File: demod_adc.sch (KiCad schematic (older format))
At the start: 0 parts

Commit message: Finished filters page, started demod
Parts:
- added C?: 0.1uF, ~, symbol C
- added R? (x2): 2.2k, ~, symbol R
- added T?: TRANSFO2, ~, symbol TRANSFO2
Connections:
- new net: C?.2, R?.1, R?.2, T?.2 (AB)
- new net: T?.4 (SB), T?.5 (SC)
- new net +5V: R?.1
- new net AGND: C?.1, R?.2
- new net ft_ana: T?.1 (AA)
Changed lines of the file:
@@
 LIBS:cmos4000
 LIBS:adc-dac
-LIBS:memory
 LIBS:special
 LIBS:analog_switches
@@
 LIBS:tsop
 LIBS:varistor
-LIBS:vishay
-LIBS:vishay_tsal4400_bpw85c
-LIBS:vishay-1
 LIBS:v-reg
-LIBS:v-reg-2
-LIBS:v-reg-fairchild
-LIBS:v-reg-lowdrop
 LIBS:si570
 LIBS:blackrock_components
@@
 $Descr A4 11693 8268
 encoding utf-8
-Sheet 1 5
+Sheet 5 5
 Title ""
-Date "16 oct 2014"
+Date "19 oct 2014"
 Rev ""
 Comp ""
@@
 Comment4 ""
 $EndDescr
+$Comp
+L +5V #PWR?
+U 1 1 54442E3F
+P 1700 1500
+F 0 "#PWR?" H 1700 1590 20  0001 C CNN
+F 1 "+5V" H 1700 1590 30  0000 C CNN
+F 2 "" H 1700 1500 60  0000 C CNN
+F 3 "" H 1700 1500 60  0000 C CNN
+	1    1700 1500
+	1    0    0    -1
+$EndComp
+$Comp
+L AGND #PWR?
+U 1 1 54442E45
+P 1050 2350
+F 0 "#PWR?" H 1050 2350 40  0001 C CNN
+F 1 "AGND" H 1050 2250 50  0000 C CNN
+F 2 "" H 1050 2350 60  0000 C CNN
+F 3 "" H 1050 2350 60  0000 C CNN
+	1    1050 2350
+	1    0    0    -1
+$EndComp
+$Comp
+L C C?
+U 1 1 54442E4B
+P 1350 2150
+F 0 "C?" V 1400 2250 40  0000 L CNN
+F 1 "0.1uF" V 1400 1900 40  0000 L CNN
+F 2 "~" H 1388 2000 30  0000 C CNN
+F 3 "~" H 1350 2150 60  0000 C CNN
+	1    1350 2150
+	0    -1   -1   0
+$EndComp
+Connection ~ 1650 2150
+Wire Wire Line
+	1550 2150 2550 2150
+Wire Wire Line
+	1050 2150 1050 2350
+Wire Wire Line
+	1150 2150 1050 2150
+$Comp
+L R R?
+U 1 1 54442E55
+P 1700 1850
+F 0 "R?" V 1780 1850 40  0000 C CNN
+F 1 "2.2k" V 1707 1851 40  0000 C CNN
+F 2 "~" V 1630 1850 30  0000 C CNN
+F 3 "~" H 1700 1850 30  0000 C CNN
+	1    1700 1850
+	1    0    0    -1
+$EndComp
+$Comp
+L R R?
+U 1 1 54442E5B
+P 1650 2450
+F 0 "R?" V 1730 2450 40  0000 C CNN
+F 1 "2.2k" V 1657 2451 40  0000 C CNN
+F 2 "~" V 1580 2450 30  0000 C CNN
+F 3 "~" H 1650 2450 30  0000 C CNN
+	1    1650 2450
+	1    0    0    -1
+$EndComp
+Wire Wire Line
+	1700 1500 1700 1600
+$Comp
+L AGND #PWR?
+U 1 1 54442E62
+P 1650 2750
+F 0 "#PWR?" H 1650 2750 40  0001 C CNN
+F 1 "AGND" H 1650 2650 50  0000 C CNN
+F 2 "" H 1650 2750 60  0000 C CNN
+F 3 "" H 1650 2750 60  0000 C CNN
+	1    1650 2750
+	1    0    0    -1
+$EndComp
+Wire Wire Line
+	1650 2700 1650 2750
+$Comp
+L TRANSFO2 T?
+U 1 1 54442E69
+P 2950 1950
+F 0 "T?" H 2950 2450 70  0000 C CNN
+F 1 "TRANSFO2" H 2950 1450 70  0000 C CNN
+F 2 "~" H 2950 1950 60  0000 C CNN
+F 3 "~" H 2950 1950 60  0000 C CNN
+	1    2950 1950
+	1    0    0    -1
+$EndComp
+Wire Wire Line
+	1650 2200 1650 2150
+Wire Wire Line
+	1700 2100 1700 2150
+Connection ~ 1700 2150
+Wire Wire Line
+	3350 1850 3350 2050
+Text HLabel 1250 1100 0    60   Input ~ 0
+ft_ana
+Wire Wire Line
+	1250 1100 2350 1100
+Wire Wire Line
+	2350 1100 2350 1750
+Wire Wire Line
+	2350 1750 2550 1750
 $EndSCHEMATC

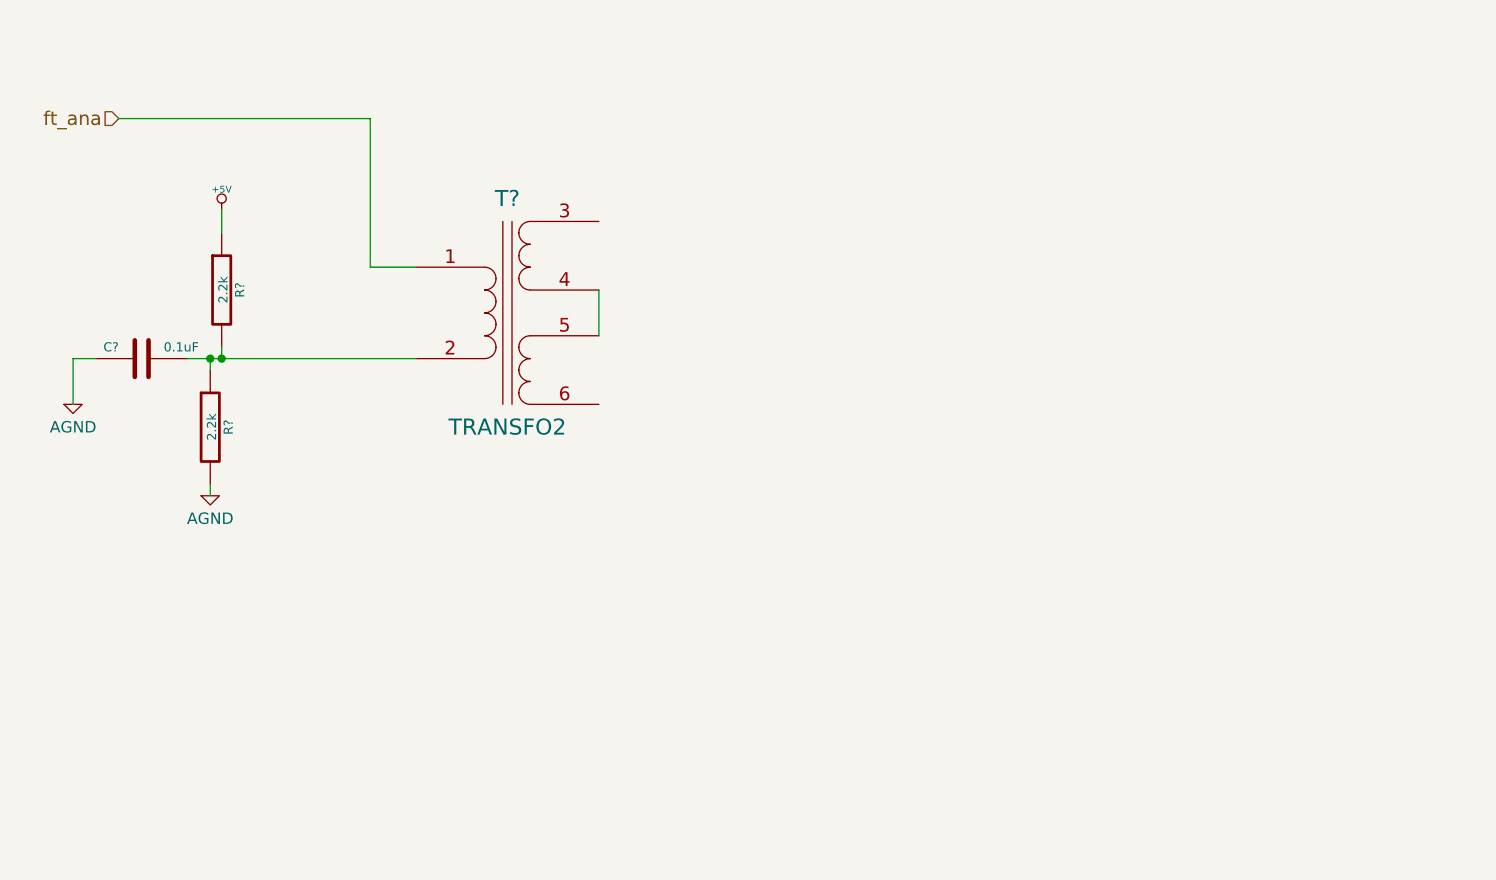
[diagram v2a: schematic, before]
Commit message: Updates to demod, need to add op-amps next
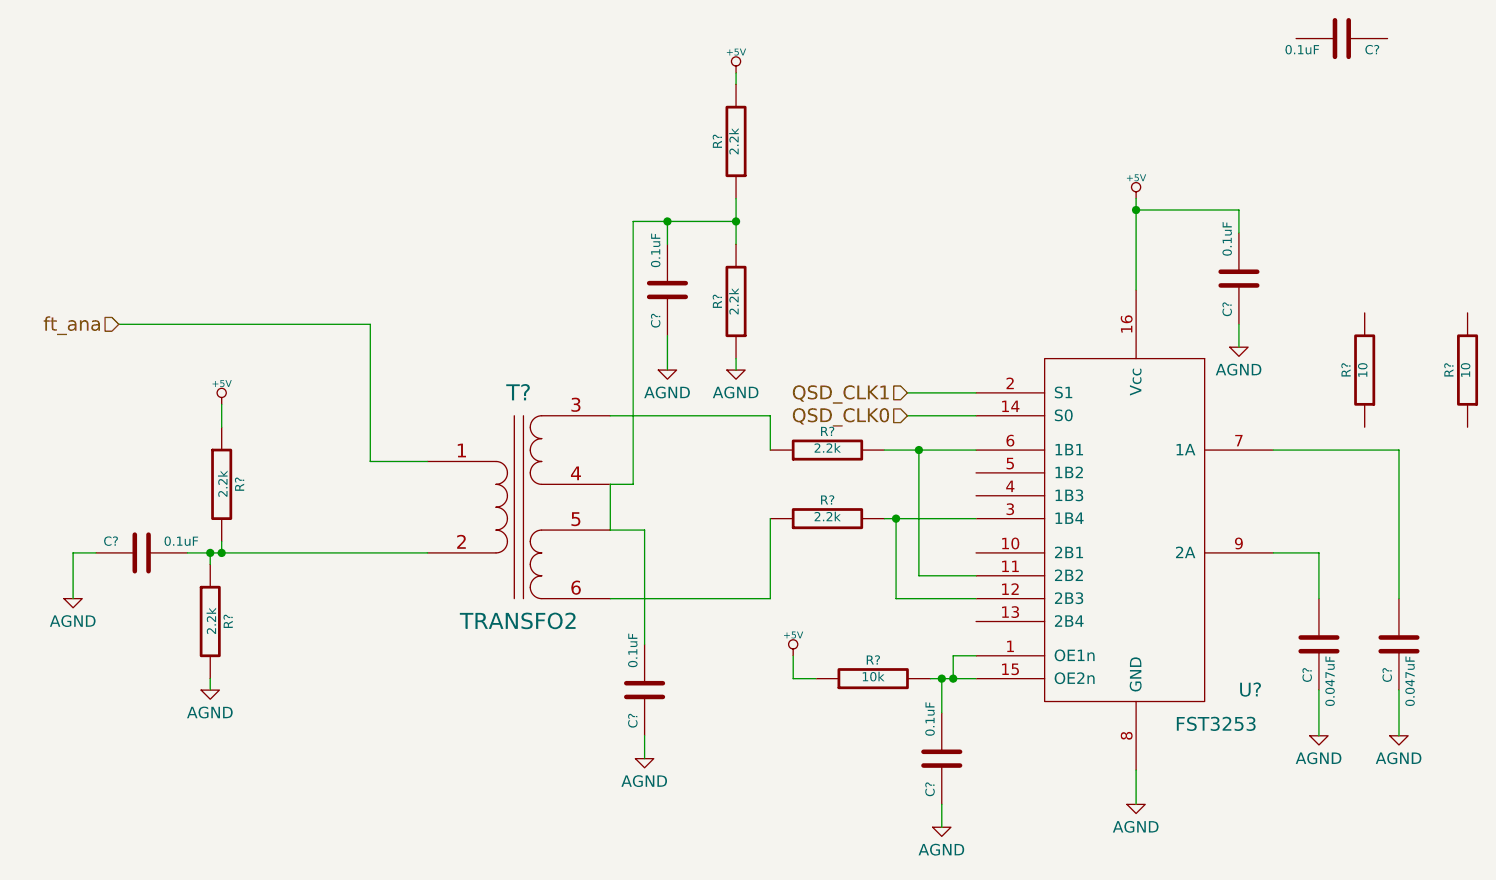
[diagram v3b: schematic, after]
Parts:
- added C? (x5): 0.1uF, ~, symbol C
- added C? (x2): 0.047uF, ~, symbol C
- added R? (x4): 2.2k, ~, symbol R
- added R?: 10k, ~, symbol R
- added R? (x2): 10, ~, symbol R
- added U?: FST3253, TSSOP16, symbol FST3253
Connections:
- net +5V: now also C?.2, R?.1, R?.2, U?.16 (Vcc)
- net AGND: now also C?.1, C?.1, C?.1, C?.1, C?.1, C?.1, R?.1, U?.8 (GND)
- net at T?.3 (SA): now also R?.1
- net at T?.4 (SB), T?.5 (SC): now also C?.2, C?.2, R?.1, R?.2
- net at T?.6 (SD): now also R?.1
- new net: R?.2, U?.11 (2B2), U?.6 (1B1)
- new net: R?.2, U?.12 (2B3), U?.3 (1B4)
- new net: C?.2, U?.9 (2A)
- new net: C?.2, R?.2, U?.1 (OE1n), U?.15 (OE2n)
- new net: C?.2, U?.7 (1A)
- new net QSD_CLK0: U?.14 (S0)
- new net QSD_CLK1: U?.2 (S1)
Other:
- moved on the sheet: C?, R?, T?
